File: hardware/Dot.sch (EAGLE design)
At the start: 36 parts, among them IC1 CAT24M010TS, IC2 SI1145, U1 ATMEGA328P-MU-QFN32, U2 TMP102, U3 ISL29125, U4 9DoF IMU, U5 BMP18

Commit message: Rearranging files
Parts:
- removed C6: 1uF, resistor:C-EUC0603
- removed C9: 100uf, Seeed-OPL-Capacitor:TANTALUM-SMD-100UF-6.3V(AVX-A)
- removed SJ1: SOLDERJUMPERNO, SparkFun:SOLDERJUMPERNO
- added C10: 1500uF 4V, adafruit:CPOL-USCT7343
- added C5: 100uf, Seeed-OPL-Capacitor:TANTALUM-SMD-100UF-6.3V(AVX-A)
- added C7: 1uF, resistor:C-EUC0603
- added JP3, JP4: JUMPER-SMT_2_NO_NO-SILK, SparkFun-Jumpers:JUMPER-SMT_2_NO_NO-SILK
- added R1, R9: (no value), resistor:R-EU_R0603
- added SJ3: SOLDERJUMPERNC2, SparkFun:SOLDERJUMPERNC2
- added U$2: DIODE-ZENER-BZT52, SparkFun:DIODE-ZENER-BZT52
- added Y1: (no value), SparkFun-Clocks:RESONATORSMD-3.2X1.3
- R5: value 130Ω -> 67Ω
- R6, R8: value 30Ω -> 67Ω
- U$3: value AT45DB641E -> AT25SF081; device AT45DB641E:AT45DB641E -> AT25SF081:AT25SF081
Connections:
- removed net INT_RGB: U1.PB6(XTAL1/TOSC1/PCINT6), U3.!INT
- removed net INT_UV: IC2.INT, U1.PB7(XTAL2/TOSC2/PCINT7)
- removed net N$2: IC1.A1, SJ1.1
- removed net TEMP_ALERT: U1.PB2(SS/OC1B/PCINT2), U2.ALERT
- new net INT_MULTIPLE: IC2.INT, R7A.1, U1.PB2(SS/OC1B/PCINT2), U2.ALERT, U3.!INT
- new net N$5: C7.2, JP1.7, JP3.2
- new net N$6: U1.PB6(XTAL1/TOSC1/PCINT6), Y1.3
- new net N$8: U1.PB7(XTAL2/TOSC2/PCINT7), Y1.1
- new net VIN_PIN: JP1.6, JP4.1, R9.2
- net +3V3: now also C10.+, C5.+, R7A.2, SJ3.2, U$2.C, U$3.NHOLD, U$3.WP; no longer C6.1, C9.+, SJ1.2, U$3.NRST
- net GND: now also C10.-, C5.-, R1.1, U$2.A, Y1.2; no longer C6.2, C9.-, U$3.PAD
- net LED: now also R5.2; no longer R8.2
- net RST: now also C7.1, JP3.1; no longer JP1.7
- net RXD: now also R6.2; no longer R5.2
- net TXD: now also R8.2; no longer R6.2
- net VIN: now also JP4.2, R1.2, R9.1, SJ3.1; no longer JP1.6
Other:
- note added: "Added 100uF Cap."
- note added: "Only needed in solar-powered Design"
- note added: "Use AT25SF081-MAHF-T"
- note added: "Use a *Schottky* diode instead of R9 for Solar-cell powered design"
- note added: "Use https://goo.gl/ZxW9QR"
- note added: "Voltage Divider Lower R"
- note removed: "Added 100uF Cap. Should soften discharge of batetry to peaks up to 30mA for 1ms. Reacharges in 175ms."
- note removed: "use AT45DB641E-MHN-Y for starndard page size (1056b/page) or AT45DB641E-MHN2B-T for binary page size (1024b/page)"
- moved on the sheet: JP1

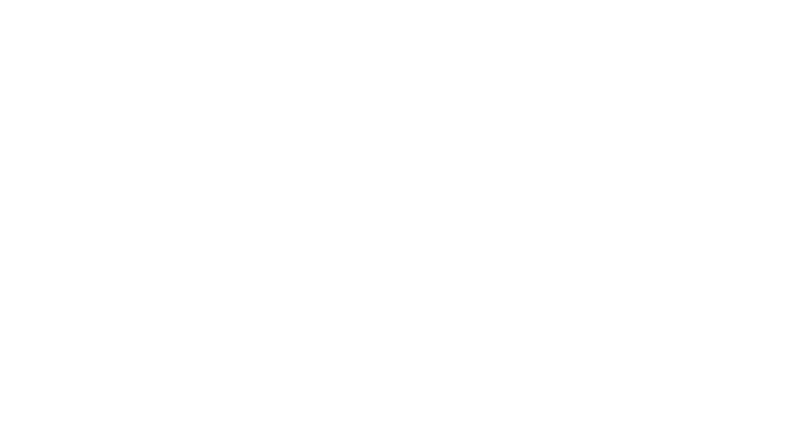
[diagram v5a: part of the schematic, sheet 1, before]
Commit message: Added MOSFET and pins for external on/off
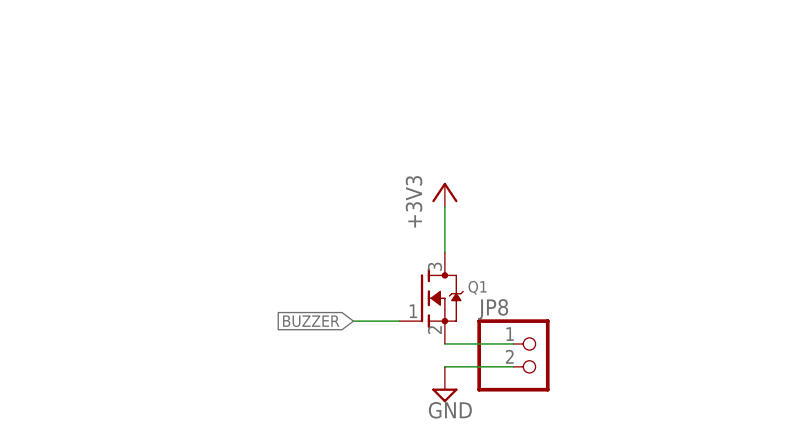
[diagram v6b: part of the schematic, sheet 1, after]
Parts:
- added JP8: (no value), pinhead:PINHD-1X2
- added Q1: (no value), adafruit:MOSFET-NREFLOW
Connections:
- new net N$16: JP8.1, Q1.S
- net +3V3: now also Q1.D
- net BUZZER: now also Q1.G
- net GND: now also JP8.2
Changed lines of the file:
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@@
 <part name="JP4" library="SparkFun-Jumpers" deviceset="JUMPER-SMT_2_NO" device="_NO-SILK"/>
 <part name="U$3" library="AT25SF081" deviceset="AT25SF081" device=""/>
+<part name="Q1" library="adafruit" deviceset="MOSFET-N" device="REFLOW"/>
+<part name="JP8" library="pinhead" deviceset="PINHD-1X2" device=""/>
+<part name="SUPPLY31" library="supply2" deviceset="GND" device=""/>
+<part name="+3V1" library="supply1" deviceset="+3V3" device=""/>
 </parts>
 <sheets>
@@
 <instance part="JP4" gate="G$1" x="-43.18" y="147.32" rot="MR270"/>
 <instance part="U$3" gate="G$1" x="71.12" y="68.58"/>
+<instance part="Q1" gate="G$1" x="205.74" y="-124.46"/>
+<instance part="JP8" gate="G$1" x="218.44" y="-132.08"/>
+<instance part="SUPPLY31" gate="GND" x="208.28" y="-134.62"/>
+<instance part="+3V1" gate="G$1" x="208.28" y="-111.76"/>
 </instances>
 <busses>
@@
 <pinref part="Y1" gate="G$1" pin="2"/>
 <pinref part="SUPPLY30" gate="GND" pin="GND"/>
+</segment>
+<segment>
+<pinref part="JP8" gate="G$1" pin="2"/>
+<wire x1="215.9" y1="-132.08" x2="208.28" y2="-132.08" width="0.1524" layer="91"/>
+<pinref part="SUPPLY31" gate="GND" pin="GND"/>
 </segment>
 </net>
@@
 <junction x="-2.54" y="166.37"/>
 </segment>
+<segment>
+<pinref part="+3V1" gate="G$1" pin="+3V3"/>
+<pinref part="Q1" gate="G$1" pin="D"/>
+<wire x1="208.28" y1="-114.3" x2="208.28" y2="-119.38" width="0.1524" layer="91"/>
+</segment>
 </net>
 <net name="ADCENA" class="0">
@@
 <wire x1="-43.18" y1="66.04" x2="-43.18" y2="73.66" width="0.1524" layer="91"/>
 <label x="-43.18" y="73.66" size="1.27" layer="95" xref="yes"/>
+</segment>
+<segment>
+<pinref part="Q1" gate="G$1" pin="G"/>
+<wire x1="203.2" y1="-127" x2="198.12" y2="-127" width="0.1524" layer="91"/>
+<label x="198.12" y="-127" size="1.27" layer="95" rot="R180" xref="yes"/>
 </segment>
 </net>
@@
 </segment>
 </net>
+<net name="N$16" class="0">
+<segment>
+<pinref part="JP8" gate="G$1" pin="1"/>
+<wire x1="215.9" y1="-129.54" x2="208.28" y2="-129.54" width="0.1524" layer="91"/>
+<pinref part="Q1" gate="G$1" pin="S"/>
+</segment>
+</net>

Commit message: Moved Miso via away from the 4.7kOhm array, moved graphics further apart
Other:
- note added: "Ext Oscillator - Low Fuse : 0x5F"
- note removed: "Added 100uF Cap."
- note removed: "Corrected RGB Led layout."
- note removed: "Diff to v1.3"
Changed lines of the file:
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@@
 <text x="48.26" y="78.74" size="1.016" layer="91">D = Direction</text>
 <text x="76.2" y="58.42" size="1.27" layer="91">0x68 / yes</text>
+<text x="5.08" y="27.94" size="1.778" layer="91">Ext Oscillator - Low Fuse : 0x5F</text>
 </plain>
 <instances>
-</instances>
-<busses>
-</busses>
-<nets>
-</nets>
-</sheet>
-<sheet>
-<plain>
-<text x="-13.97" y="88.9" size="2.54" layer="91">Diff to v1.3</text>
-<text x="-13.462" y="80.01" size="2.1844" layer="91">Corrected RGB Led layout.</text>
-<text x="-12.7" y="73.66" size="2.1844" layer="91">Added 100uF Cap.</text>
-</plain>
-<instances>
